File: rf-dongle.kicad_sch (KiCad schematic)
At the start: 38 parts, among them J1 USB_A, SW1 SW_Push, U1 NRF52840-QIAA-R7, X1 32MHz, X2 32.768kHz

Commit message: update product numbers and bom
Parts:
- AE1: JLC PN C89334 -> (none); Mfr. No (none) -> 2450AT18A0100001E; Mouser No (none) -> 609-2450AT18A0100001
- C1, C17, C18, C2: Mfr. No (none) -> 04023U120GAT2A; Mouser No (none) -> 581-04023U120GAT2A
- C11: Mfr. No (none) -> 04026A101JAT2A; Mouser No (none) -> 581-04026A101JAT2A
- C12, C5, C7, C8: Mfr. No (none) -> 0402X7R104KT7AT; Mouser No (none) -> 581-0402X7R104KT7AT
- C14, C15: Mfr. No (none) -> CM105X7R105K16ATH; Mouser No (none) -> 346-CM105X7R105K16A
- C19: Mfr. No (none) -> C1608X7S1A475K080AC; Mouser No (none) -> 810-C1608X7S1A475KAC
- C20, C6: Mfr. No (none) -> 06036C475KAT2A; Mouser No (none) -> 581-06036C475KAT2A
- C3: Mfr. No (none) -> VJ0402D0R8VXBAJHT; Mouser No (none) -> 77-VJ0402D0R8VXBAJHT
- C4: Mfr. No (none) -> VJ0402D0R5VXBAJHT; Mouser No (none) -> 77-VJ0402D0R5VXBAJHT
- C9: now not fitted
- D1: JLC PN C5337179 -> (none); Mfr. No (none) -> PRTR5V0U2X,215; Mouser No (none) -> 771-PRTR5V0U2X-T/R
- D2: JLC PN C165980 -> (none); Mfr. No (none) -> 599-1A10-147F; Mouser No (none) -> 645-599-1A10-147F
- D3: JLC PN C165979 -> (none); Mfr. No (none) -> 599-1A40-147F; Mouser No (none) -> 645-599-1A40-147F
- L1: Mfr. No (none) -> MCL1005-4R7-R; Mouser No (none) -> 504-MCL1005-4R7-R
- R1: Mfr. No (none) -> ERJ-U02F2R20X; Mouser No (none) -> 667-ERJ-U02F2R20X
- R2: Mfr. No (none) -> ESR01MZPF1002; Mouser No (none) -> 755-ESR01MZPF1002
- R3, R4: JLC PN C784160 -> (none); Mfr. No (none) -> ESR01MZPF56R0; Mouser No (none) -> 755-ESR01MZPF56R0
- SW1: JLC PN C231329 -> (none); Mfr. No (none) -> B3U-1000P; Mouser No (none) -> 653-B3U-1000P
- U1: value NRF52840-QIAA-R7 -> NRF52840-QIAA-F-R; JLC PN C1851953 -> (none); Mfr. No (none) -> nRF52840-QIAA-F-R; Mouser No (none) -> 949-NRF52840QIAA-F-R
- X1: Mfr. No (none) -> CX2016SA32000D0WRQG1; Mouser No (none) -> 581-CX2016SA32DWRQG1
- X2: JLC PN C97603 -> (none); Mfr. No (none) -> ABS06N-32.768kHz-9-T; Mouser No (none) -> 815-ABS06N32768KHZ9T
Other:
- note added: "C9 not required for Fxx and later"
- note added: "Most of the schematic is a direct copy of the reference schematic for the QFAA layout. The only exceptions are the LEDs, programming pins and reset button. Also I removed the C22 footprint to save space on the board, at the expense of not being able to tune the antenna after producing the boards. Should probably revisit this at some point."
- note removed: "BOM: - nRF52840 QIAA (aQFN), NRF52840-QIAA-R7, 3.3474 EUR - 5v ESD protection, PRTR5V0U2X-HXY, 0.0371 EUR ? Cap. 50v 12pF C0G 1%, GJM1555C1H120FB01D, 0.0293 EUR ? Cap. 50v 100nF X7R 10%, GRM155R71H104KE14D, 0.0026 EUR ? Cap. 25v 10nF X7R 10%, GRM155R71E103KA01D, 0.0014 EUR ? Res. 62.5mW 2R2 1%, 0402WGF220KTCE, 0.0007 EUR ? Res. 62.5mW 10k 1%, 0402WGF1002TCE, 0.0004 EUR - LED 20mA 35mcd 2V Yel., B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"
- note removed: "Most of the schematic is a direct copy of the reference schematic for the QFAA layout. The only exceptions are the LEDs, programming pins and reset button."

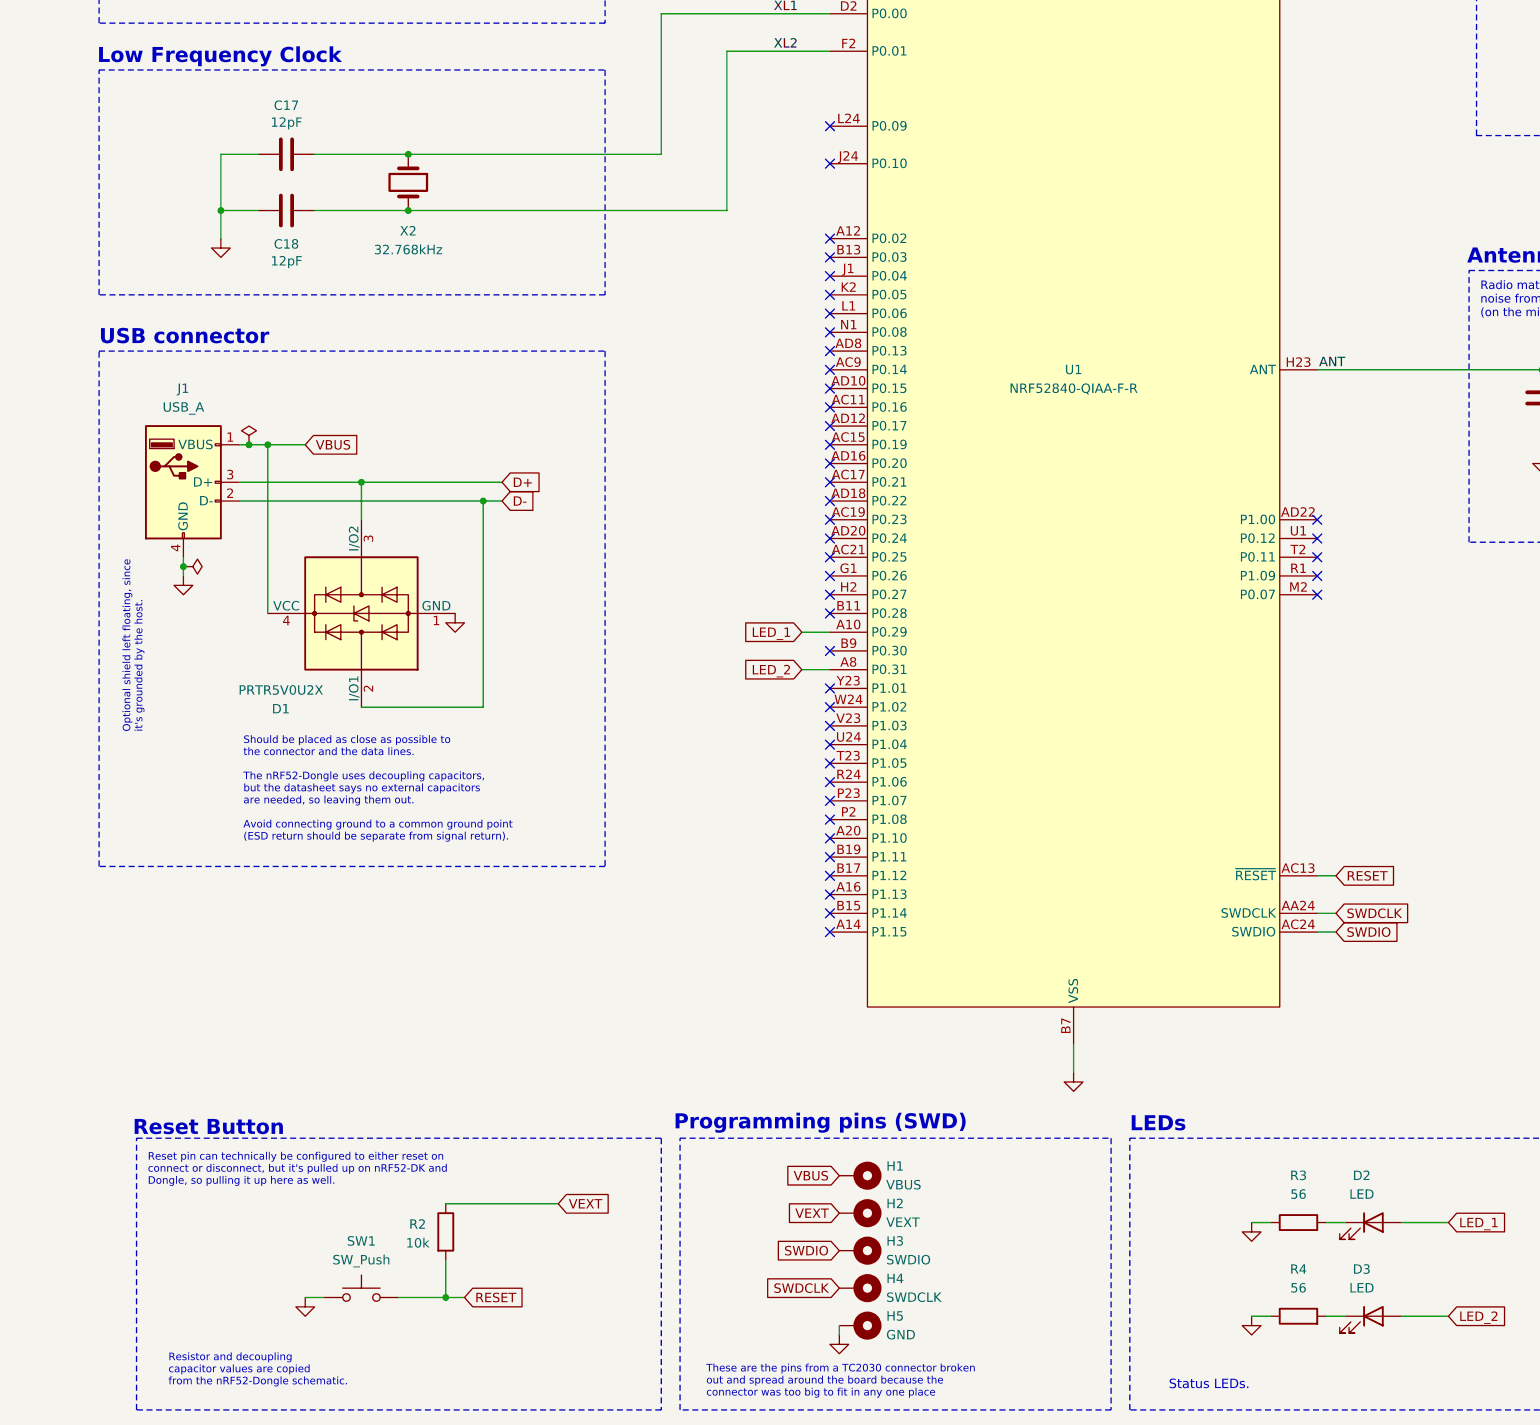
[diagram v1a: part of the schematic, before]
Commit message: cleanup USB routing, add JTAG contacts
also remove unused components and swap reset button for programmable button
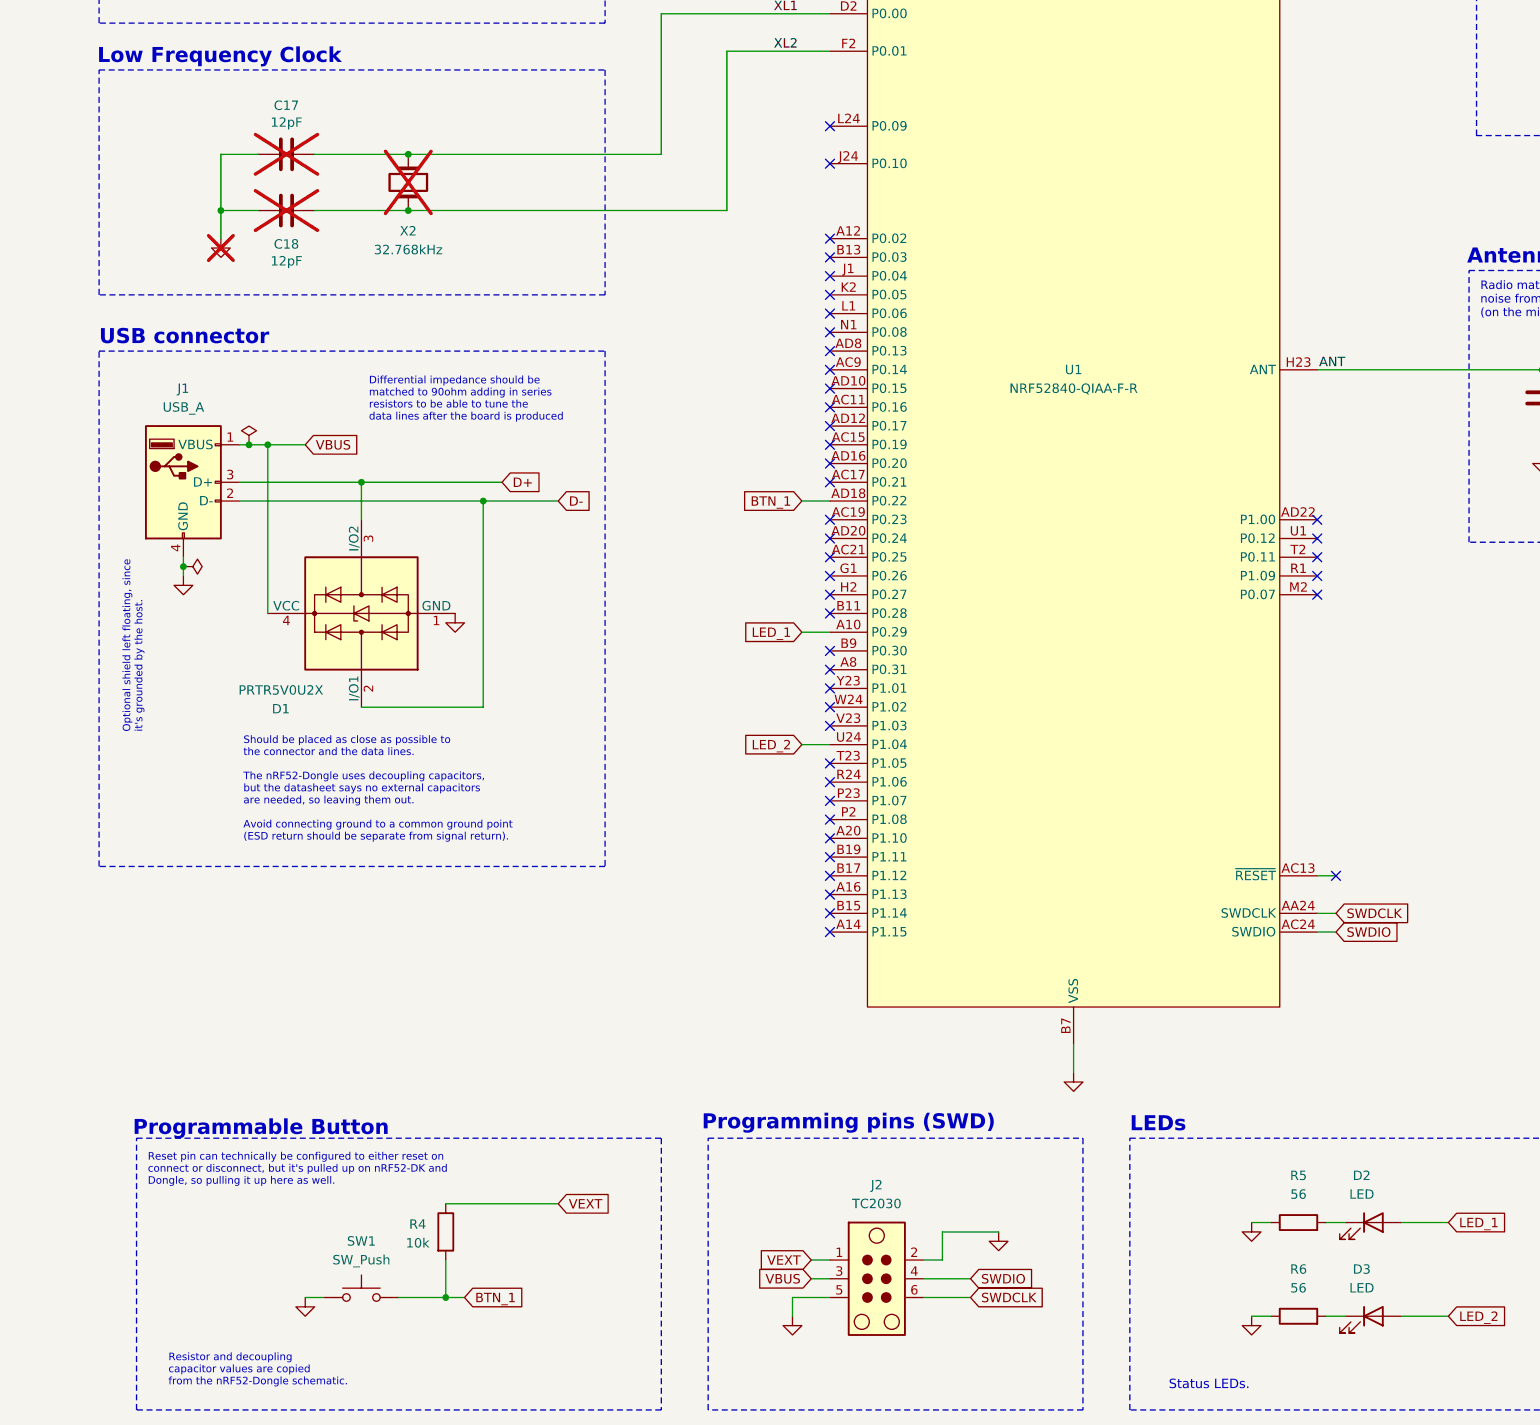
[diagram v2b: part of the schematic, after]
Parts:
- removed H1: VBUS, TestPoint:TestPoint_THTPad_D1.0mm_Drill0.5mm, symbol Mechanical:MountingHole_Pad
- removed H2: VEXT, TestPoint:TestPoint_THTPad_D1.0mm_Drill0.5mm, symbol Mechanical:MountingHole_Pad
- removed H3: SWDIO, TestPoint:TestPoint_THTPad_D1.0mm_Drill0.5mm, symbol Mechanical:MountingHole_Pad
- removed H4: SWDCLK, TestPoint:TestPoint_THTPad_D1.0mm_Drill0.5mm, symbol Mechanical:MountingHole_Pad
- removed H5: GND, TestPoint:TestPoint_THTPad_D1.0mm_Drill0.5mm, symbol Mechanical:MountingHole_Pad
- added J2: TC2030, Connector:Tag-Connect_TC2030-IDC-NL_2x03_P1.27mm_Vertical, symbol Connector:TC2030
- C17, C18, X2: now not fitted; now left out of the parts list
- C9: now left out of the parts list
- renumbered R2 to R4, R3 to R5, R4 to R6
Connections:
- net GND: now also J2.2, J2.5
- net LED_2: now also U1.U24 (P1.04); no longer U1.A8 (P0.31)
- net SWDCLK: now also J2.6
- net SWDIO: now also J2.4
- net VBUS: now also J2.3
- net VEXT: now also J2.1
- net BTN_1: now reaches U1.AD18 (P0.22)
- net BTN_1: now also R4.2, SW1.2
- removed net RESET: R4.2, SW1.2, U1.AC13 (~{RESET})
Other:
- note added: "Differential impedance should be matched to 90ohm adding in series resistors to be able to tune the data lines after the board is produced"
- note added: "Programmable Button"
- note removed: "Reset Button"
- note removed: "These are the pins from a TC2030 connector broken out and spread around the board because the connector was too big to fit in any one place"

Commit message: ordered rev 3
Reverted PCB outline to first iteration, swapped order of USB pads,
removed an optional component near the antenna, and moved around
debug pins to more easily align them with the perforated board
used to create the programming jig.
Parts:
- removed J2: TC2030, Connector:Tag-Connect_TC2030-IDC-NL_2x03_P1.27mm_Vertical, symbol Connector:TC2030
- removed R4: 10k, Resistor_SMD:R_0402_1005Metric_Pad0.72x0.64mm_HandSolder, symbol Device:R
- removed SW1: SW_Push, Button_Switch_SMD:SW_SPST_B3U-1000P, symbol Switch:SW_Push
- added H1: VBUS, TestPoint:TestPoint_THTPad_D1.0mm_Drill0.5mm, symbol Mechanical:MountingHole_Pad
- added H2: VEXT, TestPoint:TestPoint_THTPad_D1.0mm_Drill0.5mm, symbol Mechanical:MountingHole_Pad
- added H3: SWDIO, TestPoint:TestPoint_THTPad_D1.0mm_Drill0.5mm, symbol Mechanical:MountingHole_Pad
- added H4: SWDCLK, TestPoint:TestPoint_THTPad_D1.0mm_Drill0.5mm, symbol Mechanical:MountingHole_Pad
- added H5: GND, TestPoint:TestPoint_THTPad_D1.0mm_Drill0.5mm, symbol Mechanical:MountingHole_Pad
- AE1: JLC PN (none) -> C89334; Mfr. No 2450AT18A0100001E -> (none); Mouser No 609-2450AT18A0100001 -> (none)
- C1, C2: Mfr. No 04023U120GAT2A -> (none); Mouser No 581-04023U120GAT2A -> (none)
- C11: Mfr. No 04026A101JAT2A -> (none); Mouser No 581-04026A101JAT2A -> (none)
- C12, C5, C7, C8: Mfr. No 0402X7R104KT7AT -> (none); Mouser No 581-0402X7R104KT7AT -> (none)
- C14, C15: Mfr. No CM105X7R105K16ATH -> (none); Mouser No 346-CM105X7R105K16A -> (none)
- C17, C18: Mfr. No 04023U120GAT2A -> (none); Mouser No 581-04023U120GAT2A -> (none); now fitted; now in the parts list
- C19: Mfr. No C1608X7S1A475K080AC -> (none); Mouser No 810-C1608X7S1A475KAC -> (none)
- C20, C6: Mfr. No 06036C475KAT2A -> (none); Mouser No 581-06036C475KAT2A -> (none)
- C3: Mfr. No VJ0402D0R8VXBAJHT -> (none); Mouser No 77-VJ0402D0R8VXBAJHT -> (none)
- C4: Mfr. No VJ0402D0R5VXBAJHT -> (none); Mouser No 77-VJ0402D0R5VXBAJHT -> (none)
- D1: JLC PN (none) -> C5337179; Mfr. No PRTR5V0U2X,215 -> (none); Mouser No 771-PRTR5V0U2X-T/R -> (none)
- D2: JLC PN (none) -> C165980; Mfr. No 599-1A10-147F -> (none); Mouser No 645-599-1A10-147F -> (none)
- D3: JLC PN (none) -> C165979; Mfr. No 599-1A40-147F -> (none); Mouser No 645-599-1A40-147F -> (none)
- J1: now in the parts list
- L1: Mfr. No MCL1005-4R7-R -> (none); Mouser No 504-MCL1005-4R7-R -> (none)
- R1: Mfr. No ERJ-U02F2R20X -> (none); Mouser No 667-ERJ-U02F2R20X -> (none)
- R3: renamed from R5; JLC PN (none) -> C784160; Mfr. No ESR01MZPF56R0 -> (none); Mouser No 755-ESR01MZPF56R0 -> (none)
- R4: renamed from R6; JLC PN (none) -> C784160; Mfr. No ESR01MZPF56R0 -> (none); Mouser No 755-ESR01MZPF56R0 -> (none)
- U1: value NRF52840-QIAA-F-R -> NRF52840-QIAA-R7; JLC PN (none) -> C1851953; Mfr. No nRF52840-QIAA-F-R -> (none); Mouser No 949-NRF52840QIAA-F-R -> (none)
- X1: Mfr. No CX2016SA32000D0WRQG1 -> (none); Mouser No 581-CX2016SA32DWRQG1 -> (none)
- X2: JLC PN (none) -> C97603; Mfr. No ABS06N-32.768kHz-9-T -> (none); Mouser No 815-ABS06N32768KHZ9T -> (none); now fitted; now in the parts list
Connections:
- net GND: now also H5.1
- net LED_2: now also U1.A8 (P0.31); no longer U1.U24 (P1.04)
- net SWDCLK: now also H4.1
- net SWDIO: now also H3.1
- net VBUS: now also H1.1
- net VEXT: now also H2.1
- net BTN_1: no longer names the net of U1.AD18 (P0.22)
- no-connect marks 46 -> 48
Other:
- note added: "BOM: - nRF52840 QIAA (aQFN), NRF52840-QIAA-R7 - Crystal 32MHz 8pF 2.0x1.6mm, CX2016SA32000D0WRQG1 - Crystal 32.768kHz 2.0x1.2mm, ABS06N-32.768kHz-9-T - Chip ant 2.4GHz 0.5dBi, 2450AT18A100E - 5v ESD protection TVS diode, PRTR5V0U2X-HXY - Inductor 4.7nH 5% - Res. 0402 2R2 1% - Res. 0402 56 1% - Cap. 12pF C0G 0402 2% - Cap. 100nF X7R 10% - Cap. 4.7uF X7R 0603 - Cap. 0.8pF C0G 0.05% - Cap. 0.5pF C0G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"
- note added: "Most of the schematic is a direct copy of the reference schematic for the QIAA layout. The only exceptions are the LEDs and programming pins."
- note added: "The antenna should have its own matching network, used to tune the antenna's frequency, omitting it for now, since I have no way to tune the components after the PCB is produced."
- note added: "These are the pins from a TC2030 connector broken out and spread around the board because the connector was too big to fit in any one place"
- note removed: "Differential impedance should be matched to 90ohm adding in series resistors to be able to tune the data lines after the board is produced"
- note removed: "Most of the schematic is a direct copy of the reference schematic for the QFAA layout. The only exceptions are the LEDs, programming pins and reset button. Also I removed the C22 footprint to save space on the board, at the expense of not being able to tune the antenna after producing the boards. Should probably revisit this at some point."
- note removed: "Programmable Button"
- note removed: "Reset pin can technically be configured to either reset on connect or disconnect, but it's pulled up on nRF52-DK and Dongle, so pulling it up here as well."
- note removed: "Resistor and decoupling capacitor values are copied from the nRF52-Dongle schematic."
- note removed: "The antenna should have its own matching network, used to tune the antenna's frequency, omitting it for now, since I have no way to tune such the components after the PCB is produced."
- moved on the sheet: D2, D3, R3, R4
